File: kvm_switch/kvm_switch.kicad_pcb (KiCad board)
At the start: 2 copper layers, 40.2 x 14.2 mm, 18 parts, among them J1 Conn_01x04_Pin, J2 Conn_01x06_Pin, J3 Conn_02x05_Odd_Even, J4 Conn_01x06_Pin, J5 Conn_02x05_Odd_Even, U1 PC817, U2 PC817, U3 PC817

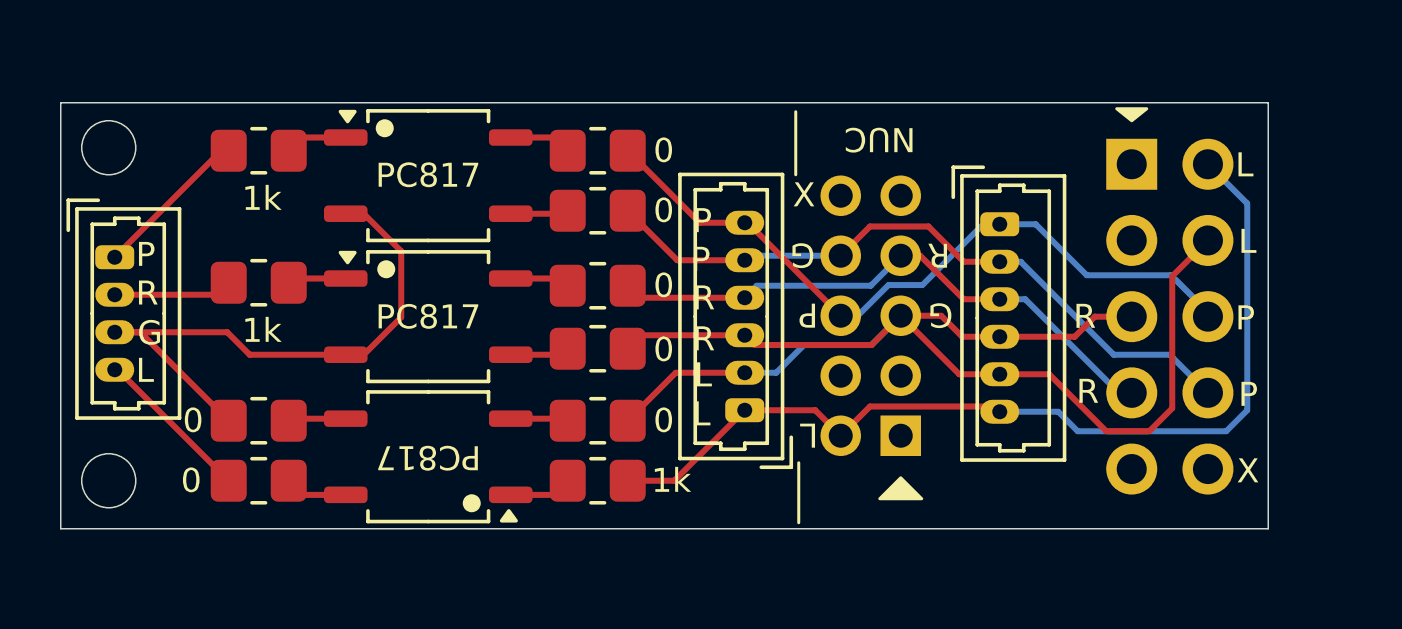
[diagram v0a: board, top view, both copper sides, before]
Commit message: PC817 패키지 타입을 SSO-4로 변경
Signed-off-by: Ju, Gyeong-min <jcmh74@gmail.com>
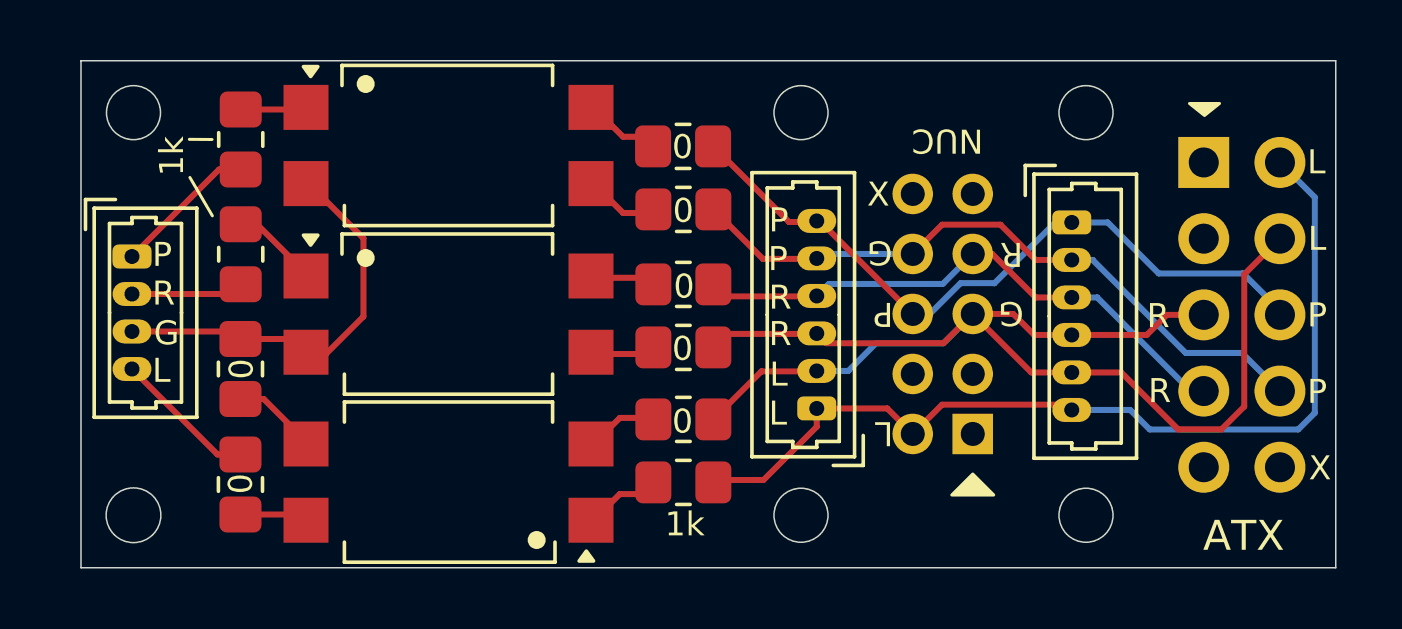
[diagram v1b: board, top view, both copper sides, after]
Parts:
- U1, U2, U3: footprint Package_SO:SOP-4_3.8x4.1mm_P2.54mm -> Package_SO:SSO-4_6.7x5.1mm_P2.54mm_Clearance8mm
- moved R7 2.85 mm to (138.5, 92.5)
- moved R10 2.85 mm to (138.5, 88.0)
- moved R3 2.85 mm to (138.5, 83.4)
- moved R6 2.85 mm to (138.5, 90.4)
- moved R9 2.85 mm to (138.5, 85.9)
- moved R2 2.85 mm to (138.4, 81.3)
- moved J3 2.40 mm to (148.1, 90.8)
- moved J2 2.40 mm to (142.9, 90.0)
- moved J4 2.40 mm to (151.4, 83.8)
- moved J5 2.40 mm to (155.8, 81.8)
- moved R4 1.83 mm to (123.7, 88.7), turned to 90 degrees
- moved U1 1.21 mm to (130.6, 81.2)
- moved R8 1.12 mm to (123.7, 84.8), turned to 90 degrees
- moved U2 1.08 mm to (130.6, 92.4)
- moved R1 0.71 mm to (123.7, 81.0), turned to 90 degrees
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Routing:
- net GND: track 20.0 -> 13.8 mm
- net Net-(R8-Pad2): track 1.96 -> 2.94 mm
- net /ATX_RSTSW_A: track 19.9 -> 19.0 mm
- net Net-(R4-Pad1): track 1.93 -> 2.86 mm
- net /ATX_PWRLED-: track 45.7 -> 44.8 mm
- net Net-(R2-Pad1): track 2.08 -> 2.85 mm
- net Net-(R3-Pad1): track 1.94 -> 2.69 mm
- net Net-(R7-Pad2): track 2.09 -> 2.82 mm
- net Net-(R6-Pad2): track 1.93 -> 2.62 mm
- net /ATX_PWRSW_A: track 24.2 -> 23.7 mm
- net /GPIO_PWRLED: track 5.33 -> 4.80 mm
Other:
- board size 40.2 x 14.2 mm -> 41.8 x 16.9 mm
